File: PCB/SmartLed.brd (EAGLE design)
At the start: 85.1 x 65.5 mm, 48 parts, among them IC2 DS1307, IC3 MEGA8-P, K1 G5LE, Q2 32.768khz, T1 BC337

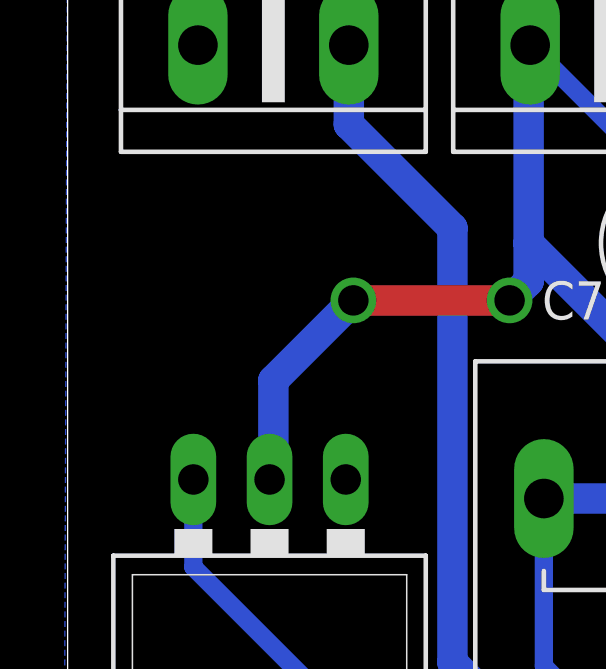
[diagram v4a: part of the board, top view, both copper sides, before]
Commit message: Add a pinhead for light sensor
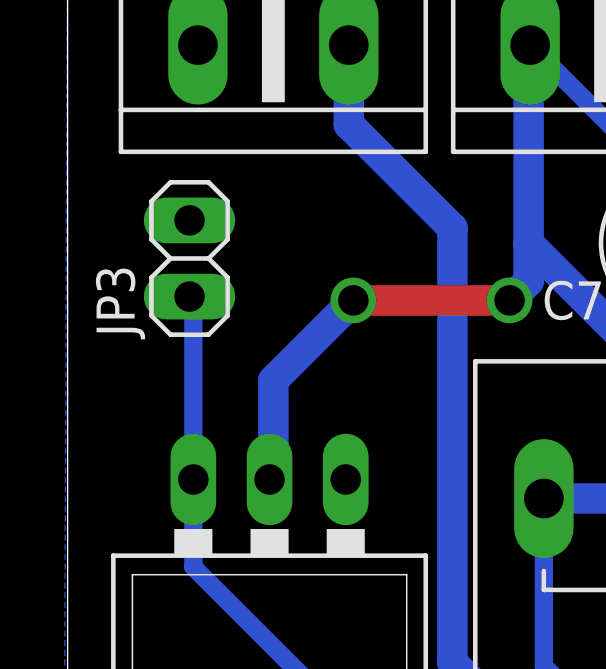
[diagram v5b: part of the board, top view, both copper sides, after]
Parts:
- added JP3: (no value), pinhead:1X02
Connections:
- net +5V: now also JP3.1
- net GND: now also JP3.2
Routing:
- net +5V: track 230.8 -> 237.0 mm
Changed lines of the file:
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@@
 <element name="JP3-PIR" library="pinhead" package="1X03" value="" x="37.846" y="74.93" rot="R180"/>
 <element name="JP1" library="pinhead" package="1X02" value="" x="30.734" y="74.93" rot="R180"/>
+<element name="JP3" library="pinhead" package="1X02" value="" x="0.508" y="87.122" rot="R90"/>
 </elements>
 <signals>
@@
 <contactref element="IC1" pad="GND"/>
 <contactref element="JP3-PIR" pad="1"/>
+<contactref element="JP3" pad="2"/>
 <wire x1="55.3466" y1="75.2348" x2="62.7126" y2="75.2348" width="0" layer="19" extent="1-1"/>
 </signal>
@@
 <wire x1="68.834" y1="55.372" x2="68.834" y2="52.832" width="0.6096" layer="16"/>
 <wire x1="68.834" y1="52.832" x2="68.072" y2="52.07" width="0.6096" layer="16"/>
+<contactref element="JP3" pad="1"/>
+<wire x1="0.508" y1="85.852" x2="0.635" y2="85.852" width="0.6096" layer="16"/>
+<wire x1="0.635" y1="85.852" x2="0.635" y2="79.756" width="0.6096" layer="16"/>
 </signal>
 <signal name="N$12">

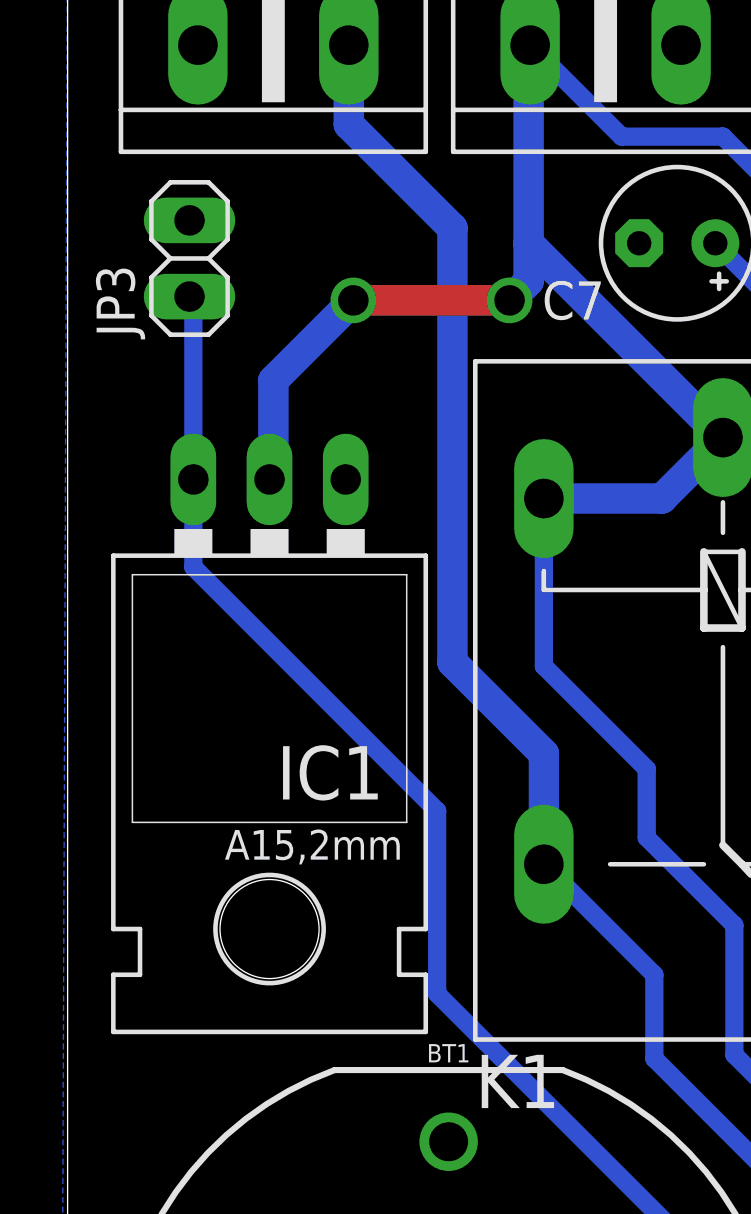
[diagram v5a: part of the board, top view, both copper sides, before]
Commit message: Fix wrong voltage regulator footprint
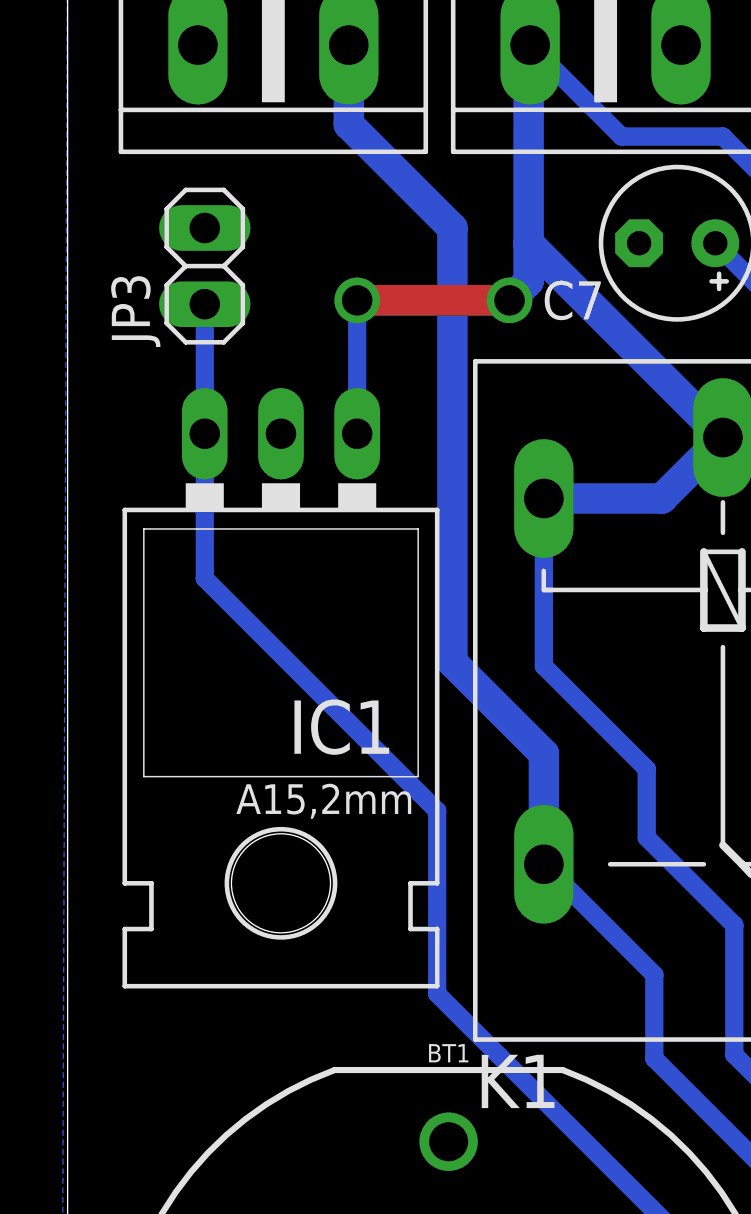
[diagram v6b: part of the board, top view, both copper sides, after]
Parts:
- IC1: device v-reg:79XXL -> v-reg:78XXL
- moved IC1 1.57 mm to (3.56, 77.5)
- moved JP3 0.57 mm to (1.02, 86.9)
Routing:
- net +12V: track 76.5 -> 73.7 mm
- net +5V: track 237.0 -> 236.4 mm
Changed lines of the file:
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@@
 <attribute name="MPN" value="" x="62.484" y="45.212" size="1.778" layer="27" rot="R90" display="off"/>
 </element>
-<element name="IC1" library="v-reg" package="79XXL" value="" x="3.175" y="75.946" rot="R180"/>
 <element name="JP3-PIR" library="pinhead" package="1X03" value="" x="37.846" y="74.93" rot="R180"/>
 <element name="JP1" library="pinhead" package="1X02" value="" x="30.734" y="74.93" rot="R180"/>
-<element name="JP3" library="pinhead" package="1X02" value="" x="0.508" y="87.122" rot="R90"/>
+<element name="JP3" library="pinhead" package="1X02" value="" x="1.016" y="86.868" rot="R90"/>
+<element name="IC1" library="v-reg" package="78XXL" value="" x="3.556" y="77.47" rot="R180"/>
 </elements>
 <signals>
@@
 <contactref element="U$1" pad="2"/>
 <contactref element="C5" pad="-"/>
-<contactref element="IC1" pad="GND"/>
 <contactref element="JP3-PIR" pad="1"/>
 <contactref element="JP3" pad="2"/>
+<contactref element="IC1" pad="GND"/>
 <wire x1="55.3466" y1="75.2348" x2="62.7126" y2="75.2348" width="0" layer="19" extent="1-1"/>
 </signal>
@@
 <wire x1="21.844" y1="83.82" x2="21.844" y2="77.216" width="0.6096" layer="16"/>
 <wire x1="21.844" y1="77.216" x2="21.082" y2="76.454" width="0.6096" layer="16"/>
-<contactref element="IC1" pad="OUT"/>
 <wire x1="29.845" y1="50.292" x2="32.385" y2="52.832" width="0.6096" layer="16"/>
-<wire x1="0.635" y1="79.756" x2="0.635" y2="76.835" width="0.6096" layer="16"/>
-<wire x1="0.635" y1="76.835" x2="8.763" y2="68.707" width="0.6096" layer="16"/>
 <wire x1="69.088" y1="65.786" x2="72.136" y2="69.342" width="0.6096" layer="16"/>
 <wire x1="72.136" y1="69.342" x2="73.66" y2="69.342" width="0.6096" layer="16"/>
@@
 <wire x1="68.834" y1="52.832" x2="68.072" y2="52.07" width="0.6096" layer="16"/>
 <contactref element="JP3" pad="1"/>
-<wire x1="0.508" y1="85.852" x2="0.635" y2="85.852" width="0.6096" layer="16"/>
-<wire x1="0.635" y1="85.852" x2="0.635" y2="79.756" width="0.6096" layer="16"/>
+<contactref element="IC1" pad="OUT"/>
+<wire x1="8.763" y1="68.707" x2="1.016" y2="76.454" width="0.6096" layer="16"/>
+<wire x1="1.016" y1="76.454" x2="1.016" y2="81.28" width="0.6096" layer="16"/>
+<wire x1="1.016" y1="85.598" x2="1.016" y2="81.28" width="0.6096" layer="16"/>
 </signal>
 <signal name="N$12">
@@
 <wire x1="18.288" y1="91.186" x2="14.9098" y2="91.186" width="0.6096" layer="16"/>
 <wire x1="14.9098" y1="91.186" x2="11.8618" y2="94.234" width="0.6096" layer="16"/>
-<contactref element="IC1" pad="IN"/>
 <wire x1="11.811" y1="94.1832" x2="11.811" y2="87.63" width="1.016" layer="16"/>
 <wire x1="11.811" y1="87.63" x2="18.288" y2="81.153" width="1.016" layer="16"/>
-<wire x1="3.302" y1="83.058" x2="5.969" y2="85.725" width="1.016" layer="16"/>
-<via x="5.969" y="85.725" extent="1-16" drill="1.016" shape="square"/>
-<wire x1="5.969" y1="85.725" x2="11.176" y2="85.725" width="1.016" layer="1"/>
+<via x="6.096" y="85.725" extent="1-16" drill="1.016" shape="square"/>
+<wire x1="6.096" y1="85.725" x2="11.176" y2="85.725" width="1.016" layer="1"/>
 <via x="11.176" y="85.725" extent="1-16" drill="1.016" shape="square"/>
 <wire x1="11.176" y1="85.725" x2="11.811" y2="86.36" width="1.016" layer="16"/>
@@
 <wire x1="15.748" y1="70.104" x2="12.319" y2="73.533" width="0.6096" layer="16"/>
 <wire x1="12.319" y1="73.533" x2="12.319" y2="79.121" width="0.6096" layer="16"/>
-<wire x1="3.302" y1="83.058" x2="3.302" y2="79.883" width="1.016" layer="16"/>
-<wire x1="3.302" y1="79.883" x2="3.175" y2="79.756" width="1.016" layer="16"/>
+<contactref element="IC1" pad="IN"/>
+<wire x1="6.096" y1="85.725" x2="6.096" y2="81.28" width="0.6096" layer="16"/>
 </signal>
 <signal name="N$8" class="1">

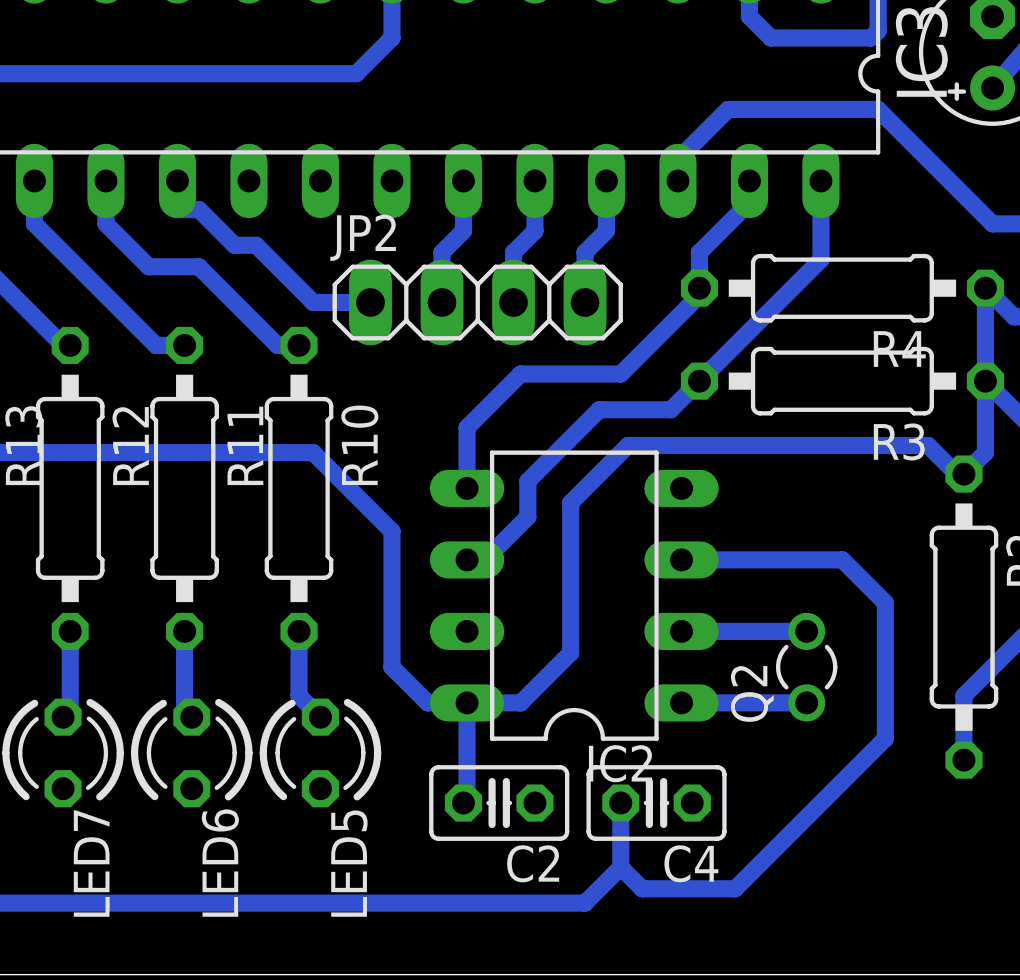
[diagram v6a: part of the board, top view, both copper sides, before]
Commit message: Add a LDR off-board sensor
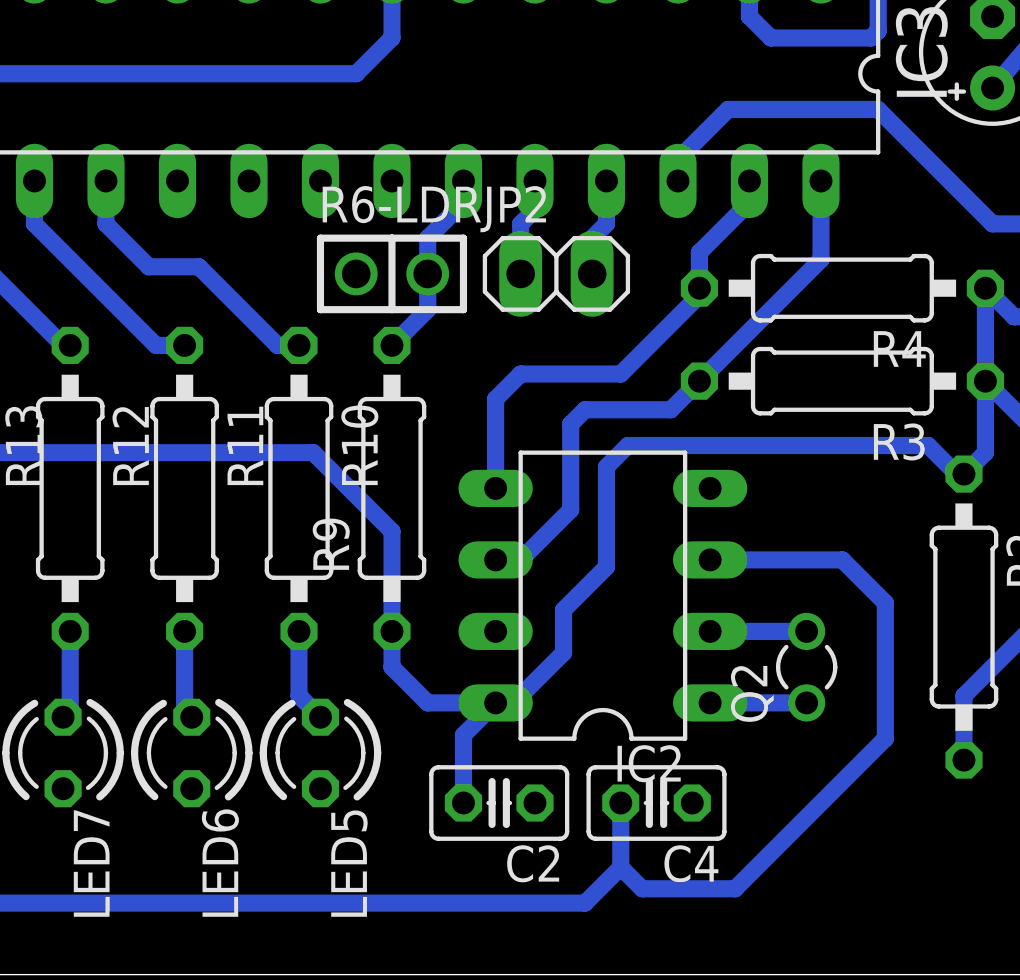
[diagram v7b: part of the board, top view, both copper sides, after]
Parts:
- added R6-LDR: PHOTOCELL1, LDR:LDR_OFFBOARD
- added R9: 10k, rcl:0207/10
- JP2: device pinhead:1X04 -> pinhead:1X02
- moved JP2 2.97 mm to (53.6, 59.2)
- moved IC2 1.02 mm to (55.2, 47.8)
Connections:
- removed net N$18: IC3.23, JP2.2
- removed net N$40: IC3.19, JP2.1
- new net N$35: IC3.23, R6-LDR.2, R9.2
- net +5V: now also R9.1
- net GND: now also R6-LDR.1
- net N$30: now also JP2.1; no longer JP2.3
- net N$34: now also JP2.2; no longer JP2.4
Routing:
- net N$40: track 9.24 -> 0.00 mm
- net N$35: track 0.00 -> 6.89 mm
- net N$18: track 5.65 -> 0.00 mm
- net N$30: track 5.65 -> 3.51 mm
- net N$34: track 5.40 -> 4.27 mm
- net N$22: track 4.45 -> 3.43 mm
- net N$21: track 4.45 -> 3.43 mm
- net N$44: track 74.5 -> 73.5 mm

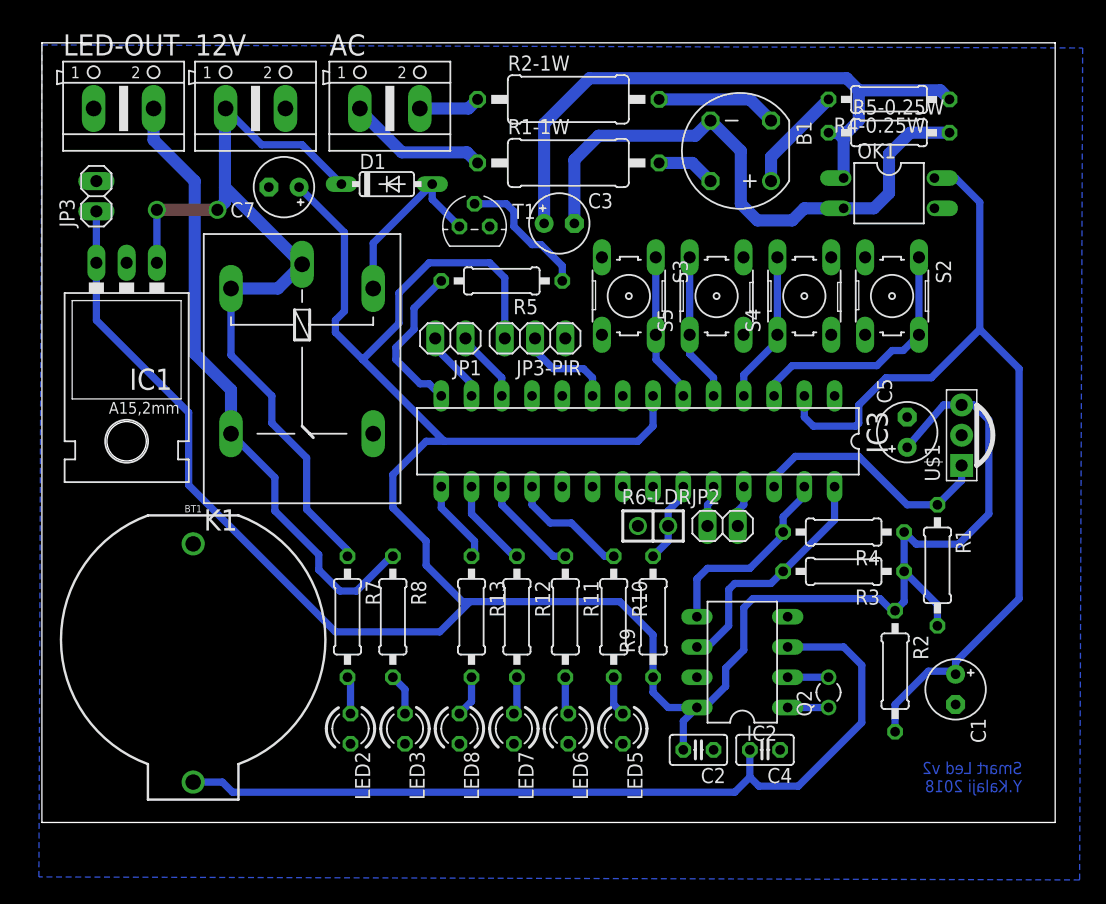
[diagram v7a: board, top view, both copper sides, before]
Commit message: Fix leds draining power from MCU I/O pins & make 12v lines thicker (after some problems caused by long time usge)
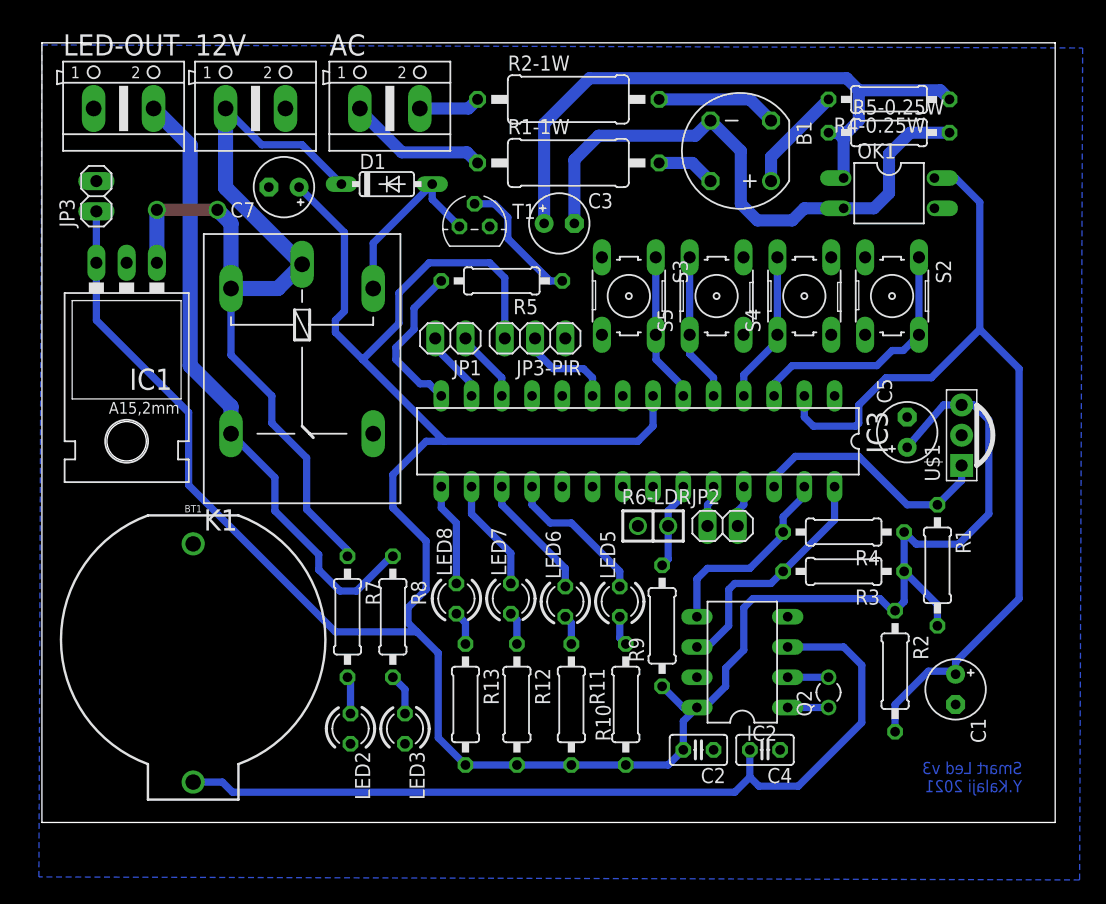
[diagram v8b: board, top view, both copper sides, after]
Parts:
- moved LED7 10.9 mm to (35.8, 53.1), turned to 90 degrees
- moved LED8 10.9 mm to (31.2, 53.1), turned to 90 degrees
- moved LED5 10.7 mm to (45.0, 52.8), turned to 90 degrees
- moved LED6 10.7 mm to (40.4, 52.8), turned to 90 degrees
- moved R10 7.44 mm to (45.5, 44.2)
- moved R11 7.38 mm to (40.9, 44.2)
- moved R13 7.38 mm to (32.0, 44.2)
- moved R12 7.37 mm to (36.3, 44.2)
- moved R9 1.08 mm to (48.5, 50.8)
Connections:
- removed net N$29: LED8.A, R13.2
- new net N$18: LED8.A, R13.1
- net +5V: now also R10.2, R11.2, R12.2, R13.2
- net GND: no longer LED5.K, LED6.K, LED7.K, LED8.K
- net N$17: now also LED8.K; no longer R13.1
- net N$20: now also LED7.K; no longer R12.1
- net N$23: now also LED7.A, R12.1; no longer LED5.A, R10.2
- net N$24: now also LED6.K; no longer R11.1
- net N$25: now also R11.1; no longer R11.2
- net N$26: now also LED5.K; no longer R10.1
- net N$27: now also LED5.A, R10.1; no longer LED7.A, R12.2
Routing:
- net +5V: track 236.9 -> 243.8 mm
- net +12V: track 73.7 -> 78.3 mm
- net N$29: track 3.47 -> 0.00 mm
- net N$18: track 0.00 -> 2.86 mm
- net N$26: track 10.2 -> 12.5 mm
- net N$24: track 8.65 -> 10.6 mm
- net N$20: track 7.57 -> 9.50 mm
- net N$17: track 7.10 -> 8.65 mm
- net N$27: track 3.15 -> 2.50 mm
- net N$25: track 3.15 -> 2.50 mm
- net N$23: track 3.36 -> 2.75 mm
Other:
- board text added: "Smart Led v3 Y.Kalaji 2021"
- board text removed: "Smart Led v2 Y.Kalaji 2018"
